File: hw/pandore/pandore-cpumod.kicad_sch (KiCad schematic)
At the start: 11 parts, among them U1 LattePanda_Mu

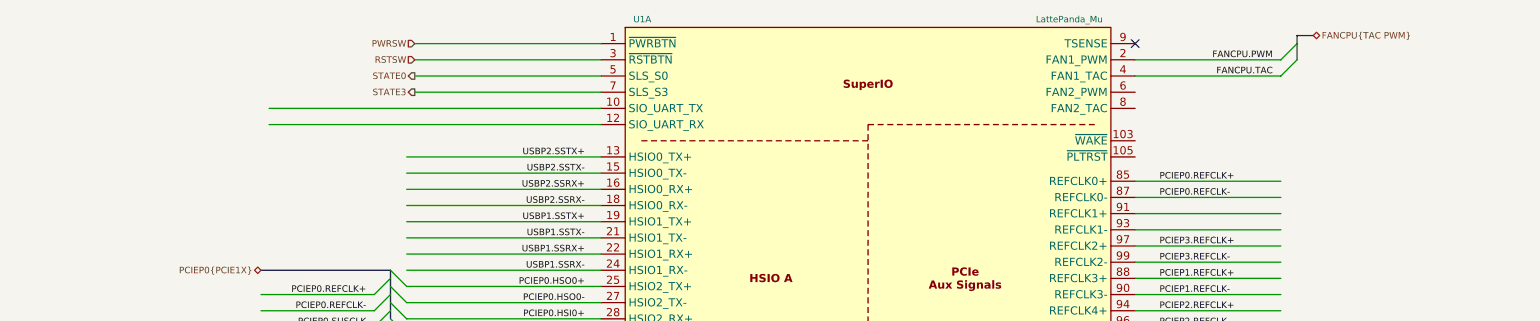
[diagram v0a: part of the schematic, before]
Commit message: more routing/placement done added 5v load switch 1A each added second fan circuit redone all diffpair routing following new stackup calc added all (?) missing connectors to unused pins
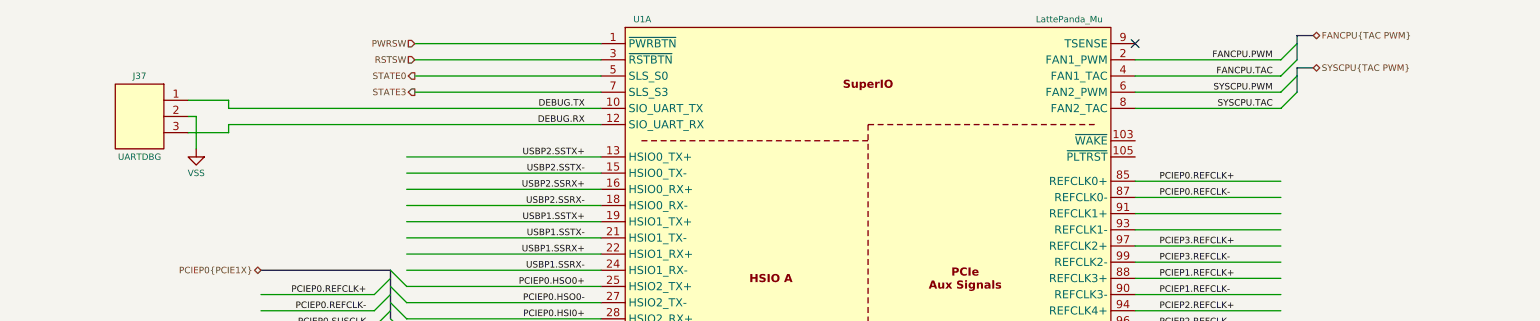
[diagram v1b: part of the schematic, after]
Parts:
- added J37: UARTDBG, reekilib_con:HDR254P1X03-TH, symbol reekilib_con:hdr-1x3
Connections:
- net VSS: now also J37.2
- net DEBUG.TX: now reaches U1.10 (SIO_UART_TX)
- net DEBUG.TX: now also J37.1
- net DEBUG.RX: now reaches U1.12 (SIO_UART_RX)
- net DEBUG.RX: now also J37.3
- net SYSCPU.PWM: now reaches U1.6 (FAN2_PWM)
- net SYSCPU.TAC: now reaches U1.8 (FAN2_TAC)

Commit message: last sprint almost done, most routing done
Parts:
- added R17, R18: ${Resistance}, ${Tolerance}, ${Power}, reekilib_res:RESC1005, symbol reekilib_res:res
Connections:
- net SUSCLK is gone; now on net PCIEP0.SUSCLK: U1.131 (SUSCLK)
- net V3P3: now also R17.1, R18.1
- net PCIEP1.~{CLKREQ}: now reaches U1.100 (~{CLKREQ3})
- net PCIEP2.~{CLKREQ}: now reaches U1.102 (~{CLKREQ4})
- net PCIEP0.~{WAKE}: now reaches U1.103 (~{WAKE})
- net PCIEP0.~{WAKE}: now also R18.2
- net PCIEP0.~{PERST}: now reaches U1.105 (~{PLTRST})
- net PCIEP0.~{PERST}: now also R17.2

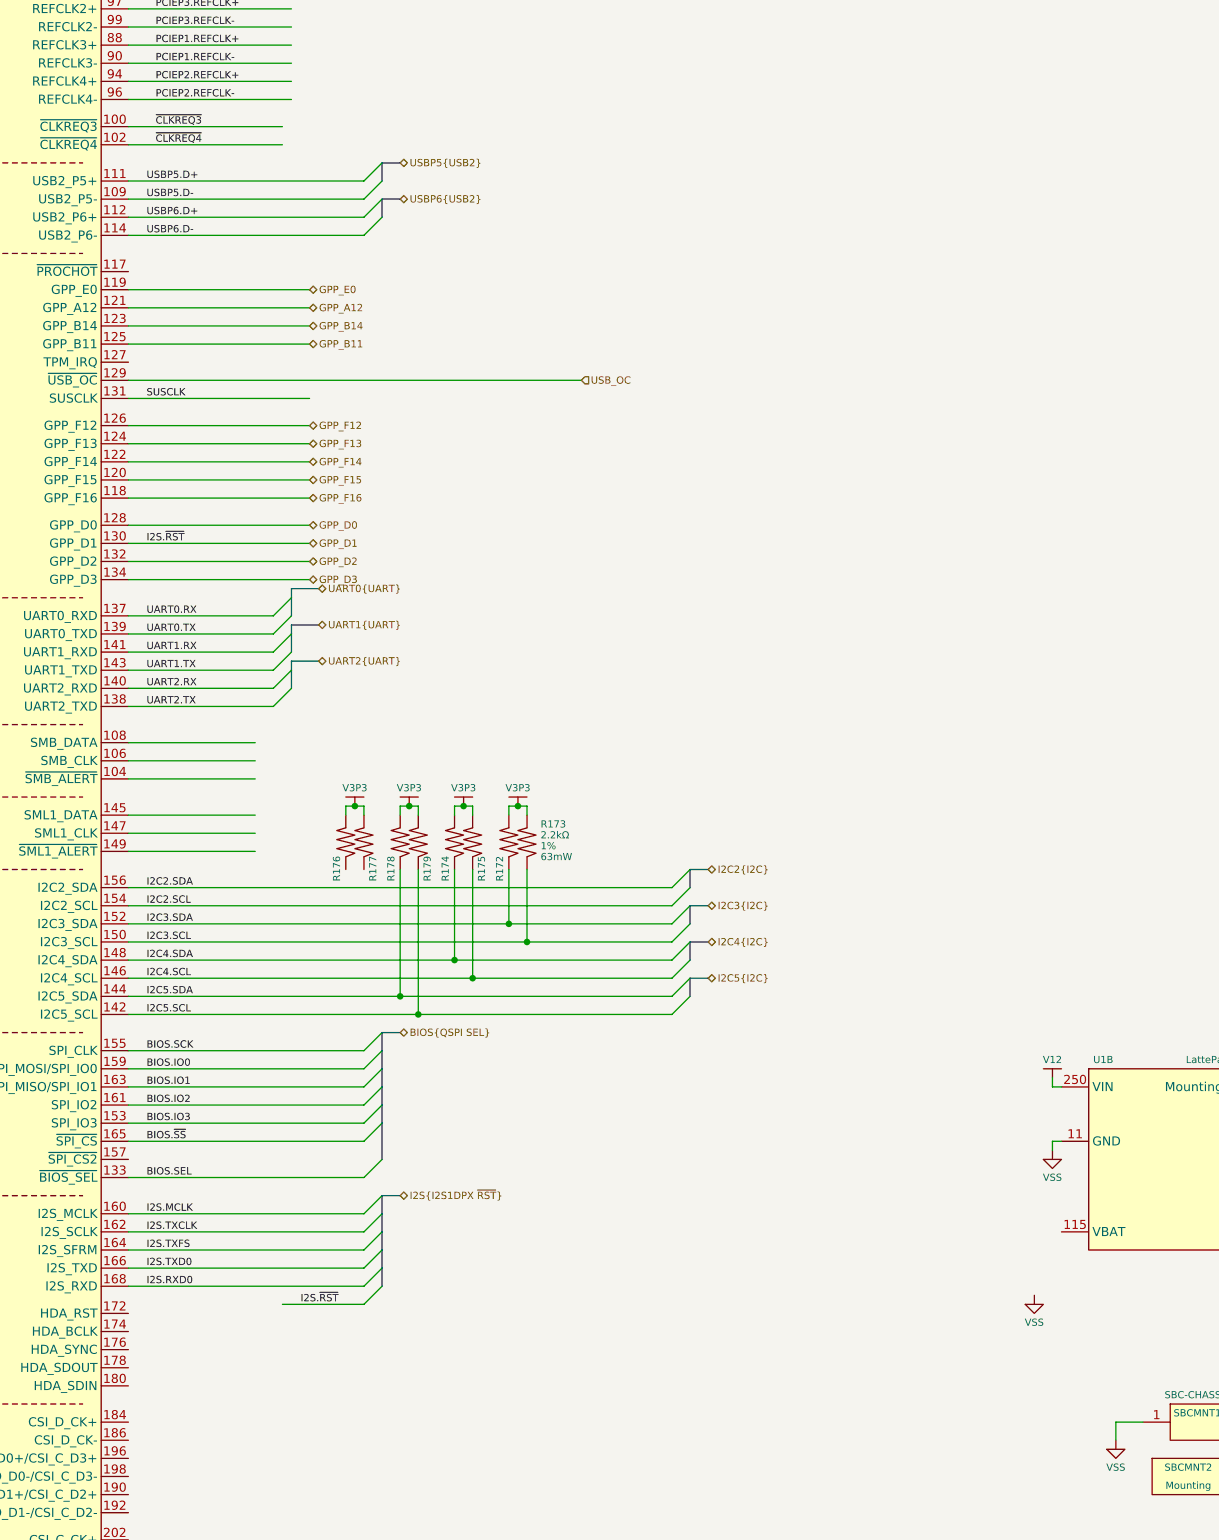
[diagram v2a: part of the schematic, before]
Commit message: finished adding mpn,mfg to all parts, finished routing placement
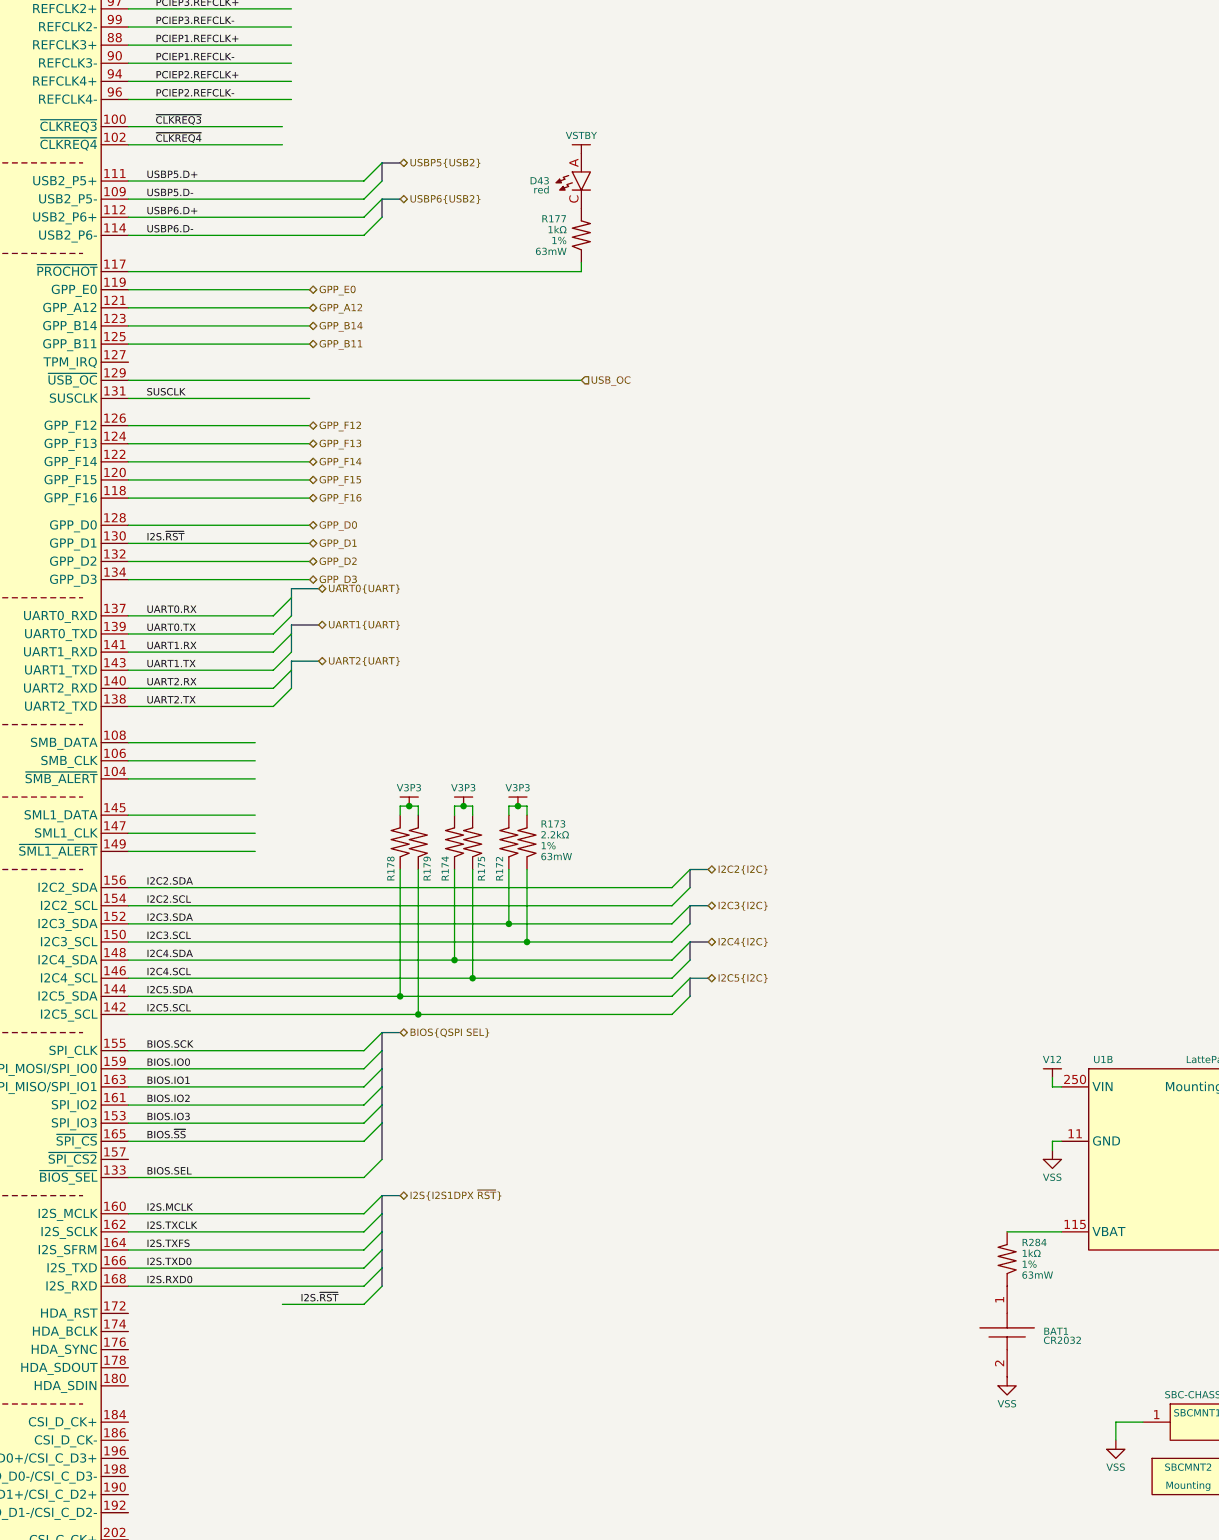
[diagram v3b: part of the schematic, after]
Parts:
- removed R176: ${Resistance}, ${Tolerance}, ${Power}, reekilib_res:RESC1005, symbol reekilib_res:res
- added BAT1: CR2032, reekilib_bat:keystone_1060, symbol reekilib_bat:batt
- added D43: ${color}, reekilib_led:LEDM1608X80, symbol reekilib_led:led
- added R284: ${Resistance}, ${Tolerance}, ${Power}, reekilib_res:RESC1005, symbol reekilib_res:res
- J37: Link url-link -> (none); MFG MFG -> Adam Tech; MPN MPN -> PH1-03-UA
- R172, R173, R174, R175, R178, R179: Link (none) -> https://yageogroup.com/products/Resistors/part/RC0402FR-072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; MFG (none) -> YAGEO; MPN (none) -> RC0402FR-072K2L
- R177: Link (none) -> https://yageogroup.com/products/Resistors/part/RC0402FR-131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; MFG (none) -> YAGEO; MPN (none) -> RC0402FR-131KL; Resistance 2.2kΩ -> 1kΩ
- U1: MFG (none) -> TE Connectivity; MPN (none) -> 2309411-1
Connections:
- net V3P3: no longer R177.1
- net VSS: now also BAT1.2 (-)
- net at R177.2: now also U1.117 (~{PROCHOT})
- net at U1.115 (VBAT): now also R284.1
- new net: D43.C, R177.1
- new net: BAT1.1 (+), R284.2
- new net VSTBY: D43.A
